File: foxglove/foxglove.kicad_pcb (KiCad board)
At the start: 4 copper layers, 70.7 x 53.3 mm, 135 parts, among them IC1 LFE5U-12F-6BG256C, J1 NEIGHBOR1, J2 NEIGHBOR2, J3 Conn_02x05_Odd_Even, J4 Conn_02x05_Odd_Even, J5 Conn_01x02_Female, J6 Conn_02x03_Odd_Even, J7 BONUS_ROW, U1 LM393, U10 SHIFTER, U11 74HC4051, U12 SHIFTER, U13 74HC4051, U14 SHIFTER, U15 74HC4051, U16 SHIFTER, U17 74HC4051, U18 SHIFTER, U19 74HC4051, U2 ADP225, U20 SHIFTER, U21 74HC4051, U22 SHIFTER, U23 74HC4051, U24 SHIFTER, U25 74LVC1G53, U3 AP2127, U4 74LVC1G3157, U5 AP2127, U6 AP2127, U7 DAC084S085, U9 74HC4051

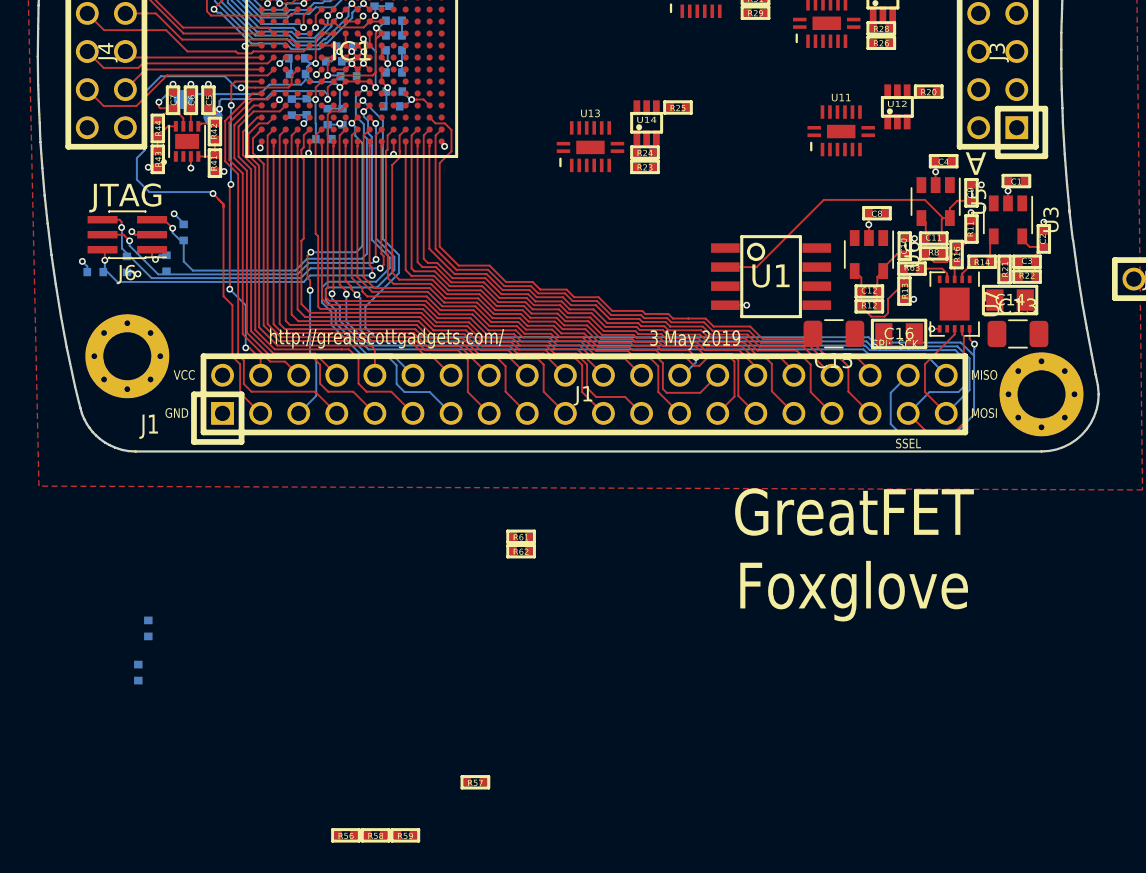
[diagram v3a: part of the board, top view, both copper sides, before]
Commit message: Corrected DAC caps, added DAC test points
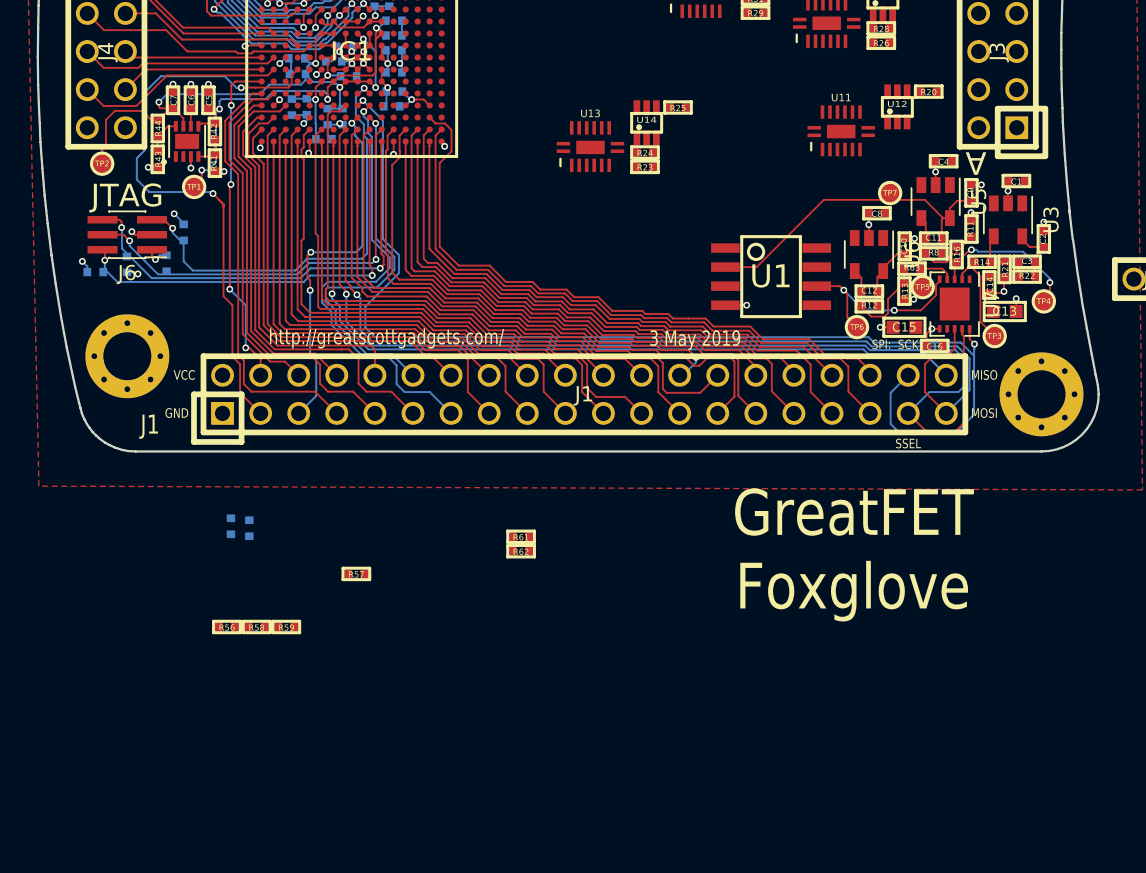
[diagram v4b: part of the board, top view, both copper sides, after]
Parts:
- added TP3: TestPoint, gsg-modules:TESTPOINT-50MIL, F.Cu at (173.4, 114.2)
- added TP4: TestPoint, gsg-modules:TESTPOINT-50MIL, F.Cu at (176.7, 111.9)
- added TP5: TestPoint, gsg-modules:TESTPOINT-50MIL, F.Cu at (168.6, 111.0)
- added TP6: TestPoint, gsg-modules:TESTPOINT-50MIL, F.Cu at (164.2, 113.6)
- added TP7: TestPoint, gsg-modules:TESTPOINT-50MIL, F.Cu at (166.4, 104.7)
- C13, C15: footprint Capacitor_SMD:C_1206_3216Metric -> gsg-modules:0603
- C14, C16: footprint gsg-modules:0805 -> gsg-modules:0402
- TP1, TP2: moved to F.Cu
- moved R58 16.0 mm to (124.2, 133.6)
- moved R57 16.0 mm to (130.8, 130.1)
- moved R59 16.0 mm to (126.2, 133.6)
- moved R56 16.0 mm to (122.2, 133.6)
- moved R6 12.1 mm to (123.7, 127.0)
- moved R3 8.76 mm to (122.5, 126.9)
- moved TP2 6.90 mm to (113.9, 102.7)
- moved TP1 4.85 mm to (120.0, 104.3)
- moved C15 4.72 mm to (167.4, 113.6)
- moved C16 2.51 mm to (169.4, 114.9)
- moved C13 1.74 mm to (174.1, 112.6)
- moved C14 1.71 mm to (173.1, 110.8), turned to 90 degrees
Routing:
- net /DAC4: track 0.00 -> 13.0 mm, vias 0 -> 2
- net /DAC2: track 1.17 -> 10.2 mm, vias 0 -> 2
- net +1V1: track 32.6 -> 38.8 mm
- net /DAC1: track 1.50 -> 7.02 mm
- net +2V5: track 22.2 -> 27.6 mm, vias 3 -> 4
- net GND: track 54.9 -> 59.9 mm, vias 43 -> 46
- net /DAC3: track 2.33 -> 3.63 mm
- net /DAC: track 22.0 -> 22.7 mm
- net /MOSI: track 65.7 -> 66.3 mm

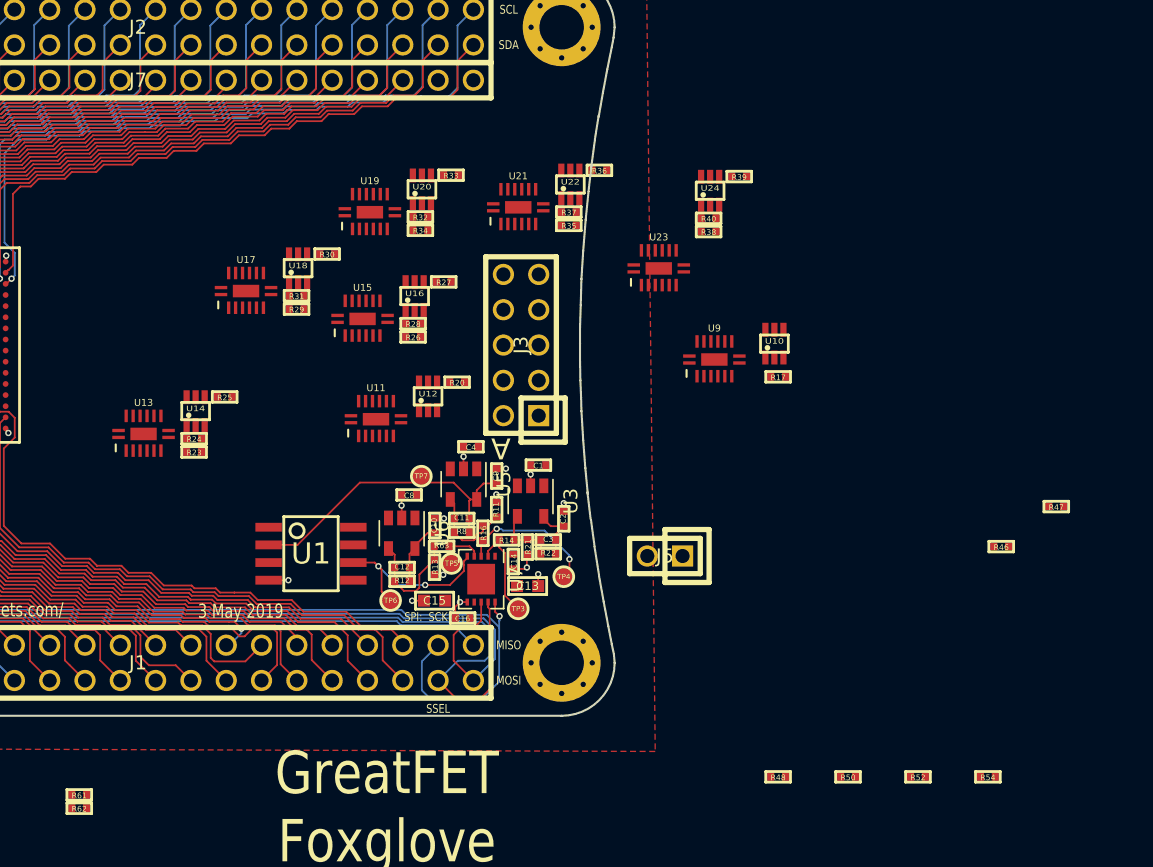
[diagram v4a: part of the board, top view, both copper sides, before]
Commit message: Began routing bank A
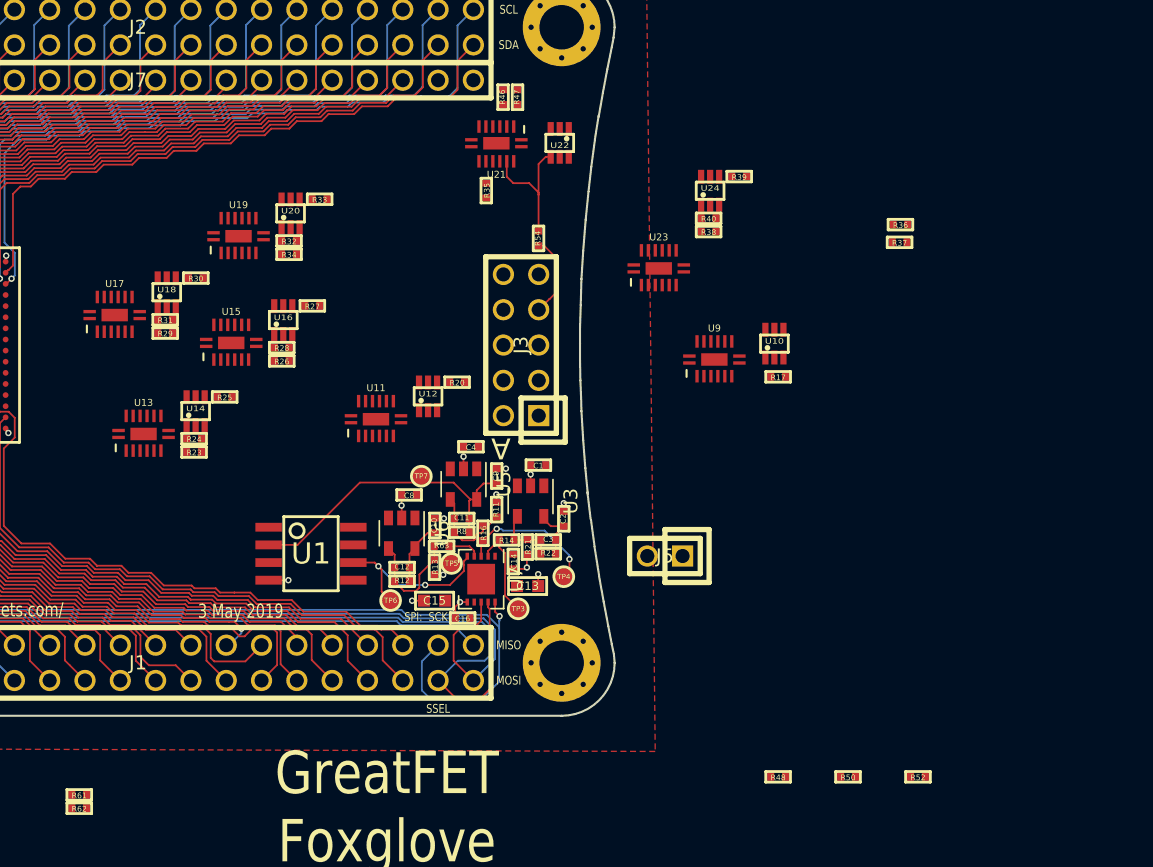
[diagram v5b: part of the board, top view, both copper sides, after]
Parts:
- moved R54 50.4 mm to (174.9, 87.6), turned to 270 degrees
- moved R47 48.7 mm to (173.4, 77.4), turned to 270 degrees
- moved R46 48.3 mm to (172.3, 77.4), turned to 270 degrees
- moved R37 23.9 mm to (200.8, 87.9)
- moved R36 22.0 mm to (200.9, 86.6)
- moved R34 9.61 mm to (156.9, 88.7)
- moved U17 9.61 mm to (144.4, 93.1)
- moved R26 9.61 mm to (156.4, 96.4)
- moved R28 9.61 mm to (156.4, 95.4)
- moved R29 9.61 mm to (148.0, 94.4)
- moved R30 9.61 mm to (150.2, 90.4)
- moved R31 9.61 mm to (148.0, 93.4)
- moved R32 9.61 mm to (156.9, 87.8)
- moved R33 9.61 mm to (159.1, 84.8)
- moved U16 9.61 mm to (156.5, 93.5)
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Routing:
- net Net-(R54-Pad1): track 0.00 -> 9.93 mm
- net /A7: track 0.00 -> 5.94 mm
